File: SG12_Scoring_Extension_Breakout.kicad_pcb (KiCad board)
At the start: 2 copper layers, 95 x 55 mm, 23 parts, among them J1 RJ45, J2 Barrel_Jack_MountingPin, J3 Barrel_Jack_MountingPin, J4 Barrel_Jack_MountingPin, J5 Barrel_Jack_MountingPin, J6 Barrel_Jack_MountingPin, J8 Conn_02x08_Odd_Even, Q1 IRF4905, Q2 IRF4905, Q3 IRF4905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

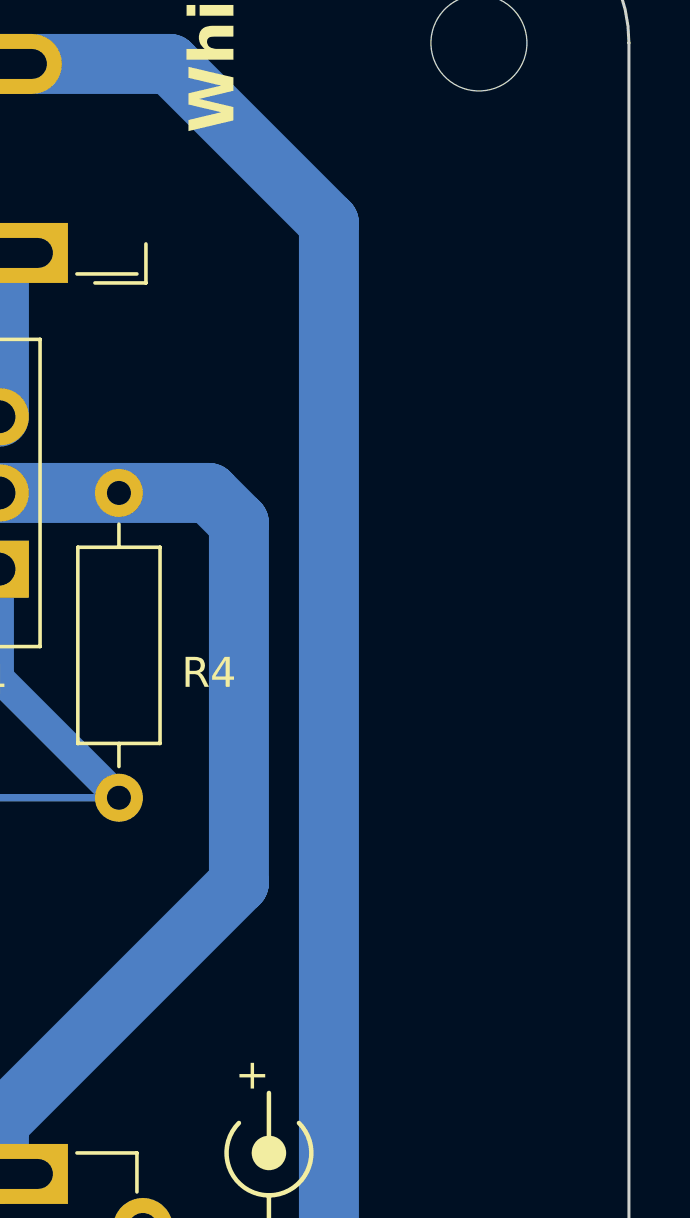
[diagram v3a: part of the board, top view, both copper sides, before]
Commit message: Added liscense to silk screen
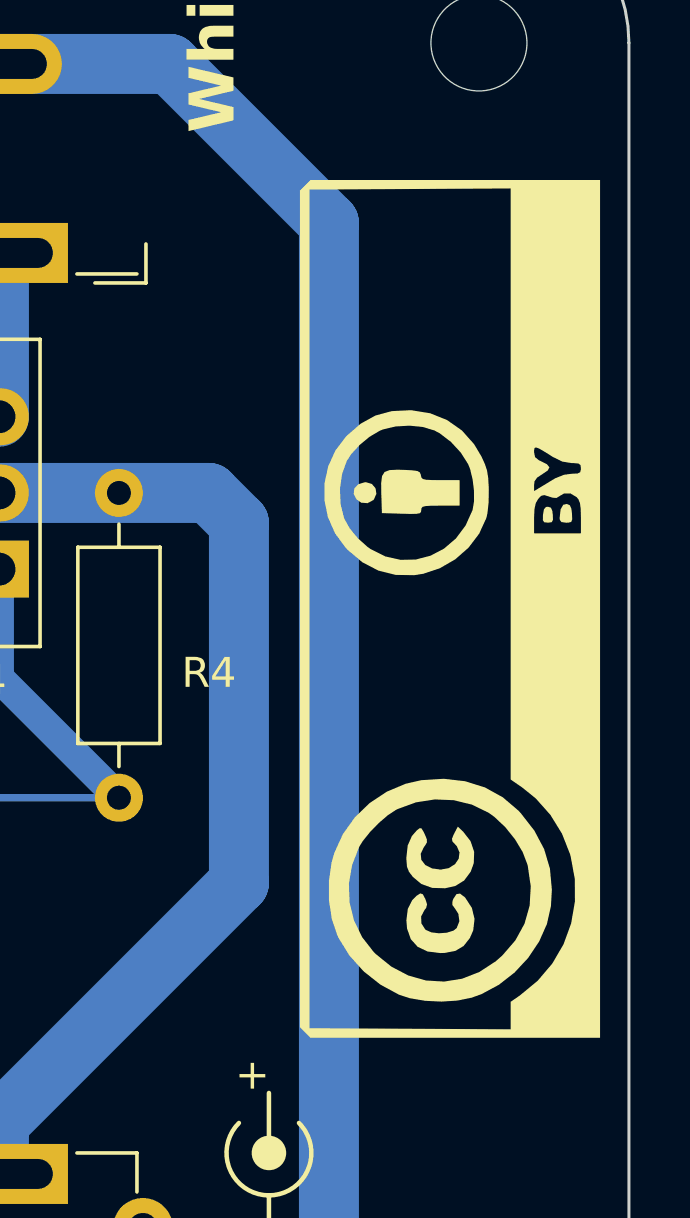
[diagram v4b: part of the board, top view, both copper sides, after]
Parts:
- added G***: LOGO, LOGO, F.Cu at (205.0, 101.9)
